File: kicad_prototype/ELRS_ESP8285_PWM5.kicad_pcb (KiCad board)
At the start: 4 copper layers, 17.5 x 24.5 mm, 48 parts, among them J1 Conn_Coaxial, J2 Conn_01x05, J3 Conn_01x05, J4 Conn_01x05, J5 Conn_Coaxial, U1 SPX3819M5-L-3-3, U2 ESP8285, U5 2450FM07D0034T, U6 SX1281, Y2 26M, Y3 52M

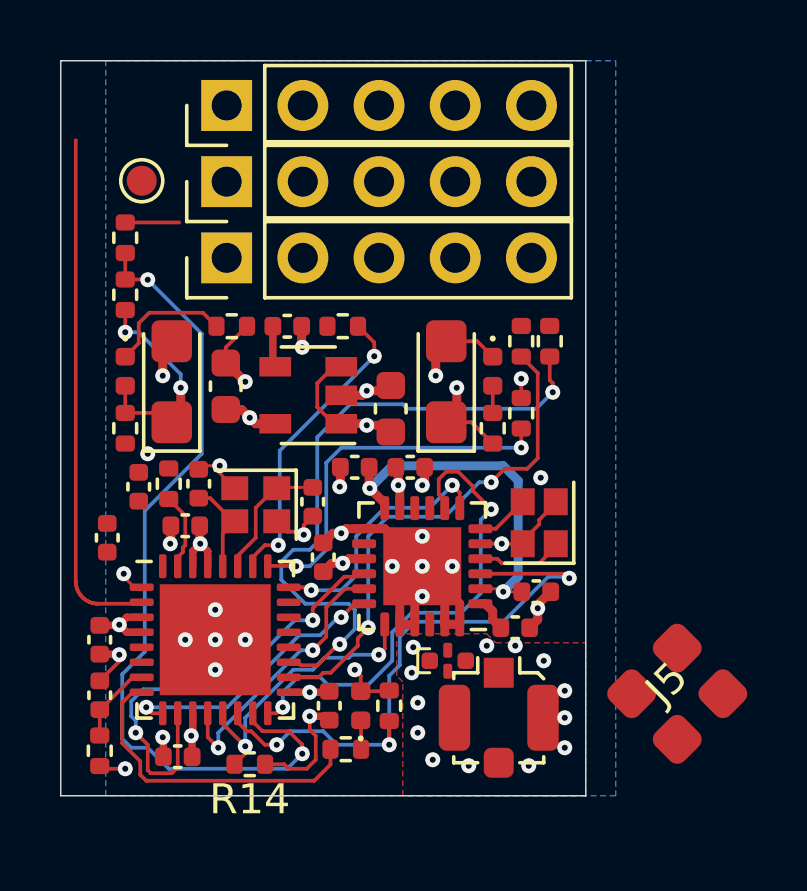
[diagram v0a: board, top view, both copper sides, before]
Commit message: move pogo pad to boot input, minor layout changes
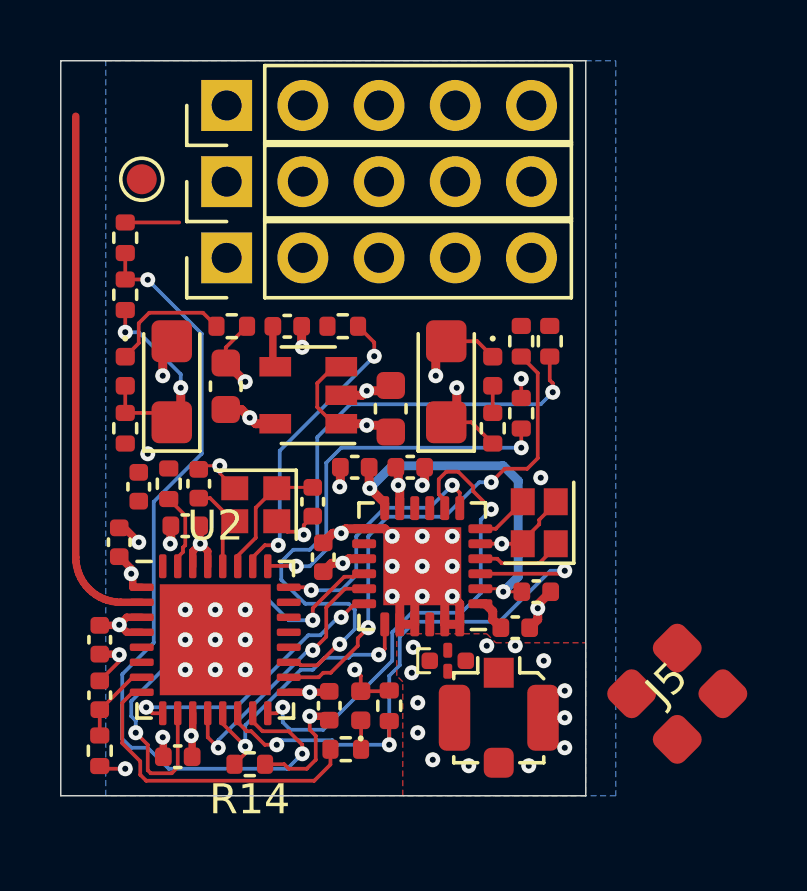
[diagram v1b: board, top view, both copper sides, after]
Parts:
- TP1: value TestPoint -> BOOT
- U2: footprint Package_DFN_QFN:QFN-32-1EP_5x5mm_P0.5mm_EP3.7x3.7mm -> ELRS_ESP8285_PWM5:QFN-32-1EP_5x5mm_P0.5mm_EP3.7x3.7mm_dense
- moved C2 0.43 mm to (159.9, 67.0)
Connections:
- TP1 pad 1: Net-(C11-Pad1) -> PWM1
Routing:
- net MISO: track 15.2 -> 17.0 mm
- net GND: track 40.0 -> 40.9 mm, vias 41 -> 50
- net +3V3: track 23.3 -> 24.0 mm
- net NRST_A: track 20.1 -> 19.6 mm

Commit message: layout work
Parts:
- moved R5 0.80 mm to (160.9, 56.9)
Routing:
- net Net-(J3-Pad3): track 0.64 -> 7.05 mm
- net Net-(C11-Pad1): track 0.29 -> 4.69 mm
- net PWM1: track 27.9 -> 31.5 mm
- net Net-(J3-Pad4): track 0.00 -> 3.22 mm
- net Net-(J3-Pad2): track 0.00 -> 2.62 mm
- net Net-(J3-Pad5): track 0.00 -> 2.52 mm
- net GND: track 40.9 -> 42.5 mm
- net Net-(J3-Pad1): track 1.80 -> 3.07 mm
- net Net-(J1-Pad1): track 0.00 -> 1.27 mm
- net Net-(U5-Pad1): track 0.00 -> 1.21 mm
